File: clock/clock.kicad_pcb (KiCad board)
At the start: 2 copper layers, 100 x 50 mm, 81 parts, among them J1 FTDI, J2 USB, J3 TP, SW1 SW_SPST, SW2 SW_SPST, SW3 SW_SPST, SW4 SW_SPST, SW5 SW_SPST, U1 iv12, U10 PCA9685PW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

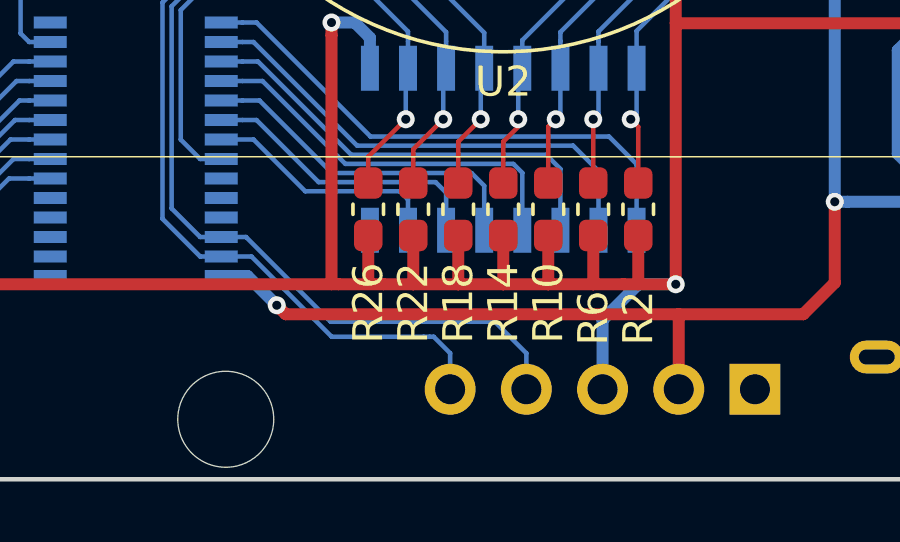
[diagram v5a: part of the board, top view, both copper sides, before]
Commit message: Moved 24v test point
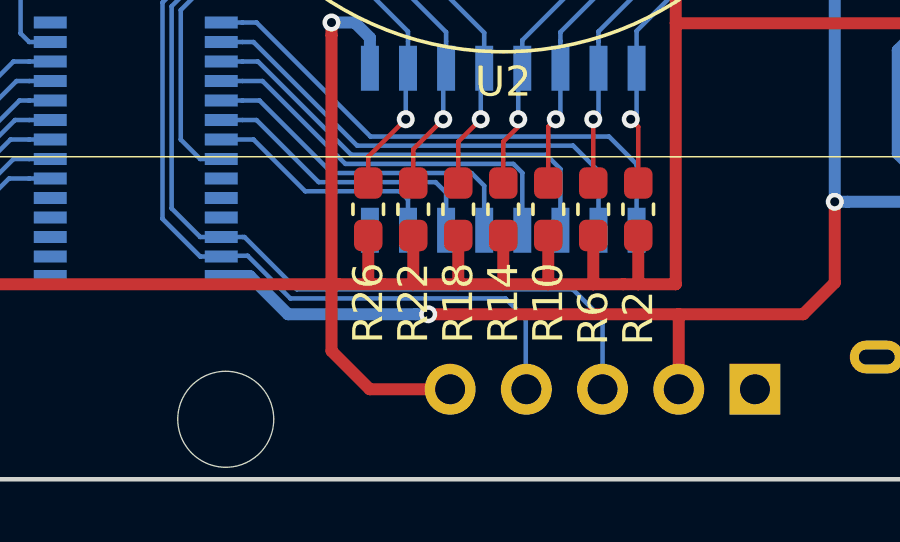
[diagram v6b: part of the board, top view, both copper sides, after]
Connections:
- J3 pad 3: +24V -> SCL
- J3 pad 4: SCL -> SDA
- J3 pad 5: SDA -> +24V
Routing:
- net SDA: track 122.3 -> 125.6 mm
- net SCL: track 126.7 -> 129.9 mm
- net +24V: track 262.7 -> 264.2 mm, vias 7 -> 6
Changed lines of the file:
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@@
     (tags "resistor handsolder")
     (attr smd)
-    (fp_text reference R39 (at 3 0.05) (layer B.SilkS)
+    (fp_text reference R39 (at -3.025 0) (layer B.SilkS)
       (effects (font (size 1 1) (thickness 0.15)) (justify mirror))
     )
@@
     (tags "resistor handsolder")
     (attr smd)
-    (fp_text reference R40 (at -3 0.1 180) (layer B.SilkS)
+    (fp_text reference R40 (at 3.025 0 180) (layer B.SilkS)
       (effects (font (size 1 1) (thickness 0.15)) (justify mirror))
     )
@@
       (net 31 +5V))
     (pad 3 thru_hole oval (at 0 -5.08 90) (size 1.7 1.7) (drill 1) (layers *.Cu *.Mask)
+      (net 73 SCL))
+    (pad 4 thru_hole oval (at 0 -7.62 90) (size 1.7 1.7) (drill 1) (layers *.Cu *.Mask)
+      (net 72 SDA))
+    (pad 5 thru_hole oval (at 0 -10.16 90) (size 1.7 1.7) (drill 1) (layers *.Cu *.Mask)
       (net 2 +24V))
-    (pad 4 thru_hole oval (at 0 -7.62 90) (size 1.7 1.7) (drill 1) (layers *.Cu *.Mask)
-      (net 73 SCL))
-    (pad 5 thru_hole oval (at 0 -10.16 90) (size 1.7 1.7) (drill 1) (layers *.Cu *.Mask)
-      (net 72 SDA))
     (model ${KISYS3DMOD}/Connector_PinHeader_2.54mm.3dshapes/PinHeader_1x05_P2.54mm_Vertical.wrl
       (at (xyz 0 0 0))
@@
   (segment (start 82.75 145.5) (end 82 145.5) (width 0.4) (layer F.Cu) (net 2))
   (segment (start 82 145.5) (end 81.500034 145.000034) (width 0.4) (layer F.Cu) (net 2))
-  (via (at 117.5 145.5) (size 0.6) (drill 0.3) (layers F.Cu B.Cu) (net 2))
   (segment (start 117.5 136.8) (end 117.5 145.5) (width 0.4) (layer F.Cu) (net 2))
   (segment (start 116.25 145.5) (end 117.5 145.5) (width 0.4) (layer F.Cu) (net 2))
-  (segment (start 116.25 145.5) (end 117.5 145.5) (width 0.4) (layer B.Cu) (net 2))
-  (segment (start 115.06 149) (end 115.06 146.69) (width 0.4) (layer B.Cu) (net 2))
-  (segment (start 115.06 146.69) (end 116.25 145.5) (width 0.4) (layer B.Cu) (net 2))
+  (segment (start 106.025 145.5) (end 106.025 147.725) (width 0.4) (layer F.Cu) (net 2))
+  (segment (start 107.3 149) (end 109.98 149) (width 0.4) (layer F.Cu) (net 2))
+  (segment (start 106.025 147.725) (end 107.3 149) (width 0.4) (layer F.Cu) (net 2))
   (via (at 91.49999 140) (size 0.6) (drill 0.3) (layers F.Cu B.Cu) (net 3))
   (segment (start 91.75 142.125) (end 91.75 140.25001) (width 0.152) (layer F.Cu) (net 3) (status 10))
@@
   (segment (start 127 144.15) (end 127 142.75) (width 0.4) (layer B.Cu) (net 31) (status 10))
   (segment (start 128 142.75) (end 127 142.75) (width 0.4) (layer B.Cu) (net 31))
-  (via (at 104.2 146.2) (size 0.6) (drill 0.3) (layers F.Cu B.Cu) (net 31))
-  (segment (start 103.225 145.225) (end 102.35 145.225) (width 0.4) (layer B.Cu) (net 31) (status 20))
-  (segment (start 104.2 146.2) (end 103.225 145.225) (width 0.4) (layer B.Cu) (net 31))
   (via (at 149.4 146.2) (size 0.6) (drill 0.3) (layers F.Cu B.Cu) (net 31))
   (segment (start 150.375 145.225) (end 151.65 145.225) (width 0.4) (layer B.Cu) (net 31) (status 20))
@@
   (segment (start 119.2 119.6) (end 119.2 122.6) (width 0.4) (layer B.Cu) (net 31))
   (segment (start 119.2 122.6) (end 120.25 123.65) (width 0.4) (layer B.Cu) (net 31))
-  (segment (start 104.2 146.2) (end 104.499999 146.499999) (width 0.4) (layer F.Cu) (net 31))
   (segment (start 117.6 149) (end 117.6 146.499999) (width 0.4) (layer F.Cu) (net 31))
-  (segment (start 104.499999 146.499999) (end 117.6 146.499999) (width 0.4) (layer F.Cu) (net 31))
   (segment (start 122.8 145.45) (end 122.8 142.749984) (width 0.4) (layer F.Cu) (net 31))
   (segment (start 117.6 146.499999) (end 121.750001 146.499999) (width 0.4) (layer F.Cu) (net 31))
@@
   (segment (start 126.574999 105.6) (end 121.45 105.6) (width 0.4) (layer B.Cu) (net 31))
   (segment (start 121.45 105.6) (end 119.25 107.8) (width 0.4) (layer B.Cu) (net 31))
+  (segment (start 108.825736 146.499999) (end 109.25 146.499999) (width 0.4) (layer B.Cu) (net 31))
+  (segment (start 103.3 145.225) (end 104.574999 146.499999) (width 0.4) (layer B.Cu) (net 31))
+  (segment (start 117.6 146.499999) (end 109.25 146.499999) (width 0.4) (layer F.Cu) (net 31))
+  (segment (start 102.35 145.225) (end 103.3 145.225) (width 0.4) (layer B.Cu) (net 31))
+  (segment (start 104.574999 146.499999) (end 108.825736 146.499999) (width 0.4) (layer B.Cu) (net 31))
+  (via (at 109.25 146.499999) (size 0.6) (drill 0.3) (layers F.Cu B.Cu) (net 31))
   (segment (start 143.125 132.776301) (end 143.0861 132.815201) (width 0.152) (layer B.Cu) (net 32) (status 30))
   (segment (start 143.125 128.5) (end 143.125 132.776301) (width 0.152) (layer B.Cu) (net 32) (status 30))
@@
   (segment (start 103.3 123.59013) (end 103.3 133.2) (width 0.152) (layer B.Cu) (net 72))
   (segment (start 100.39198 143.31898) (end 101.648 144.575) (width 0.152) (layer B.Cu) (net 72))
-  (segment (start 102.35 144.575) (end 103.356442 144.575) (width 0.152) (layer B.Cu) (net 72))
-  (segment (start 103.356442 144.575) (end 106.031442 147.25) (width 0.152) (layer B.Cu) (net 72))
-  (segment (start 106.031442 147.25) (end 109.1 147.25) (width 0.152) (layer B.Cu) (net 72))
-  (segment (start 109.432081 147.25) (end 109.3 147.25) (width 0.152) (layer B.Cu) (net 72))
-  (segment (start 109.98 147.797919) (end 109.432081 147.25) (width 0.152) (layer B.Cu) (net 72))
-  (segment (start 109.98 149) (end 109.98 147.797919) (width 0.152) (layer B.Cu) (net 72))
-  (segment (start 109.1 147.25) (end 109.3 147.25) (width 0.152) (layer B.Cu) (net 72))
   (segment (start 124.7 113.2) (end 122.75 113.2) (width 0.152) (layer B.Cu) (net 72))
   (via (at 124.7 113.2) (size 0.6) (drill 0.3) (layers F.Cu B.Cu) (net 72))
@@
   (segment (start 116.45 115.175) (end 118.075 115.175) (width 0.152) (layer B.Cu) (net 72))
   (segment (start 118.075 115.175) (end 120.05 113.2) (width 0.152) (layer B.Cu) (net 72))
+  (segment (start 112.5 148.98) (end 112.52 149) (width 0.152) (layer B.Cu) (net 72))
+  (segment (start 102.375 144.55) (end 103.230296 144.55) (width 0.152) (layer B.Cu) (net 72))
+  (segment (start 103.230296 144.55) (end 104.652294 145.971998) (width 0.152) (layer B.Cu) (net 72))
+  (segment (start 104.652294 145.971998) (end 111.821998 145.971998) (width 0.152) (layer B.Cu) (net 72))
+  (segment (start 111.821998 145.971998) (end 112.5 146.65) (width 0.152) (layer B.Cu) (net 72))
+  (segment (start 102.35 144.575) (end 102.375 144.55) (width 0.152) (layer B.Cu) (net 72))
+  (segment (start 112.5 146.65) (end 112.5 148.98) (width 0.152) (layer B.Cu) (net 72))
   (segment (start 110.875066 116.445) (end 103.604011 123.716055) (width 0.152) (layer B.Cu) (net 73))
   (segment (start 116.45 116.445) (end 110.875066 116.445) (width 0.152) (layer B.Cu) (net 73) (status 10))
@@
   (segment (start 100.695991 142.972991) (end 101.648 143.925) (width 0.152) (layer B.Cu) (net 73))
   (segment (start 103.60401 133.325926) (end 100.695991 136.233945) (width 0.152) (layer B.Cu) (net 73))
-  (segment (start 103.175 143.925) (end 102.35 143.925) (width 0.152) (layer B.Cu) (net 73))
-  (segment (start 106 146.75) (end 103.175 143.925) (width 0.152) (layer B.Cu) (net 73))
-  (segment (start 111.472081 146.75) (end 111 146.75) (width 0.152) (layer B.Cu) (net 73))
-  (segment (start 112.52 147.797919) (end 111.472081 146.75) (width 0.152) (layer B.Cu) (net 73))
-  (segment (start 112.52 149) (end 112.52 147.797919) (width 0.152) (layer B.Cu) (net 73))
-  (segment (start 111 146.75) (end 106 146.75) (width 0.152) (layer B.Cu) (net 73))
   (via (at 124.7 112.4) (size 0.6) (drill 0.3) (layers F.Cu B.Cu) (net 73))
   (segment (start 124.7 112.4) (end 122.75 112.4) (width 0.152) (layer B.Cu) (net 73))
@@
   (segment (start 156.648 143.925) (end 153.404011 140.681011) (width 0.152) (layer B.Cu) (net 73))
   (segment (start 141 112.4) (end 141.05 112.45) (width 0.152) (layer F.Cu) (net 73))
+  (segment (start 103.052 143.925) (end 102.35 143.925) (width 0.152) (layer B.Cu) (net 73))
+  (segment (start 103.125 143.925) (end 103.052 143.925) (width 0.152) (layer B.Cu) (net 73))
+  (segment (start 104.867987 145.667987) (end 103.125 143.925) (width 0.152) (layer B.Cu) (net 73))
+  (segment (start 114.067987 145.667987) (end 104.867987 145.667987) (width 0.152) (layer B.Cu) (net 73))
+  (segment (start 115.06 149) (end 115.06 146.66) (width 0.152) (layer B.Cu) (net 73))
+  (segment (start 115.06 146.66) (end 114.067987 145.667987) (width 0.152) (layer B.Cu) (net 73))
   (segment (start 131.15 126.8) (end 131.75 126.2) (width 0.4) (layer B.Cu) (net 81) (status 30))
   (segment (start 131.15 133.4) (end 131.15 126.8) (width 0.4) (layer B.Cu) (net 81) (status 30))

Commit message: Added diode polarity marks
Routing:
- net SDA: track 125.6 -> 126.4 mm
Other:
- board text added: "+"
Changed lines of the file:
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@@
   (general
     (thickness 1.6)
-    (drawings 11)
-    (tracks 902)
+    (drawings 16)
+    (tracks 903)
     (zones 0)
     (modules 81)
@@
     )
   )
+  (gr_text + (at 133.5 124.2) (layer F.SilkS)
+    (effects (font (size 1 1) (thickness 0.15)))
+  )
+  (gr_text + (at 168.8 125.8) (layer F.SilkS)
+    (effects (font (size 1 1) (thickness 0.15)))
+  )
+  (gr_text + (at 144.3 125.8) (layer F.SilkS)
+    (effects (font (size 1 1) (thickness 0.15)))
+  )
+  (gr_text + (at 113.8 125.8) (layer F.SilkS)
+    (effects (font (size 1 1) (thickness 0.15)))
+  )
+  (gr_text + (at 88.8 125.8) (layer F.SilkS)
+    (effects (font (size 1 1) (thickness 0.15)))
+  )
   (gr_text "24v\n" (at 115.1 146.2 270) (layer B.SilkS)
     (effects (font (size 1 1) (thickness 0.15)) (justify mirror))
@@
   (segment (start 124.7 113.2) (end 141 113.2) (width 0.152) (layer F.Cu) (net 72))
   (segment (start 124.7 113.2) (end 121.2 113.2) (width 0.152) (layer F.Cu) (net 72))
-  (segment (start 121.2 113.624264) (end 121.2 113.2) (width 0.152) (layer B.Cu) (net 72))
-  (segment (start 121.2 116.55) (end 121.2 113.624264) (width 0.152) (layer B.Cu) (net 72))
-  (segment (start 123.25 118.6) (end 121.2 116.55) (width 0.152) (layer B.Cu) (net 72))
   (via (at 121.2 113.2) (size 0.6) (drill 0.3) (layers F.Cu B.Cu) (net 72))
   (segment (start 120.05 113.2) (end 121.2 113.2) (width 0.152) (layer B.Cu) (net 72))
@@
   (segment (start 102.35 144.575) (end 102.375 144.55) (width 0.152) (layer B.Cu) (net 72))
   (segment (start 112.5 146.65) (end 112.5 148.98) (width 0.152) (layer B.Cu) (net 72))
+  (segment (start 121.2 113.624264) (end 121.2 113.2) (width 0.152) (layer B.Cu) (net 72))
+  (segment (start 121.2 118) (end 121.2 113.624264) (width 0.152) (layer B.Cu) (net 72))
+  (segment (start 123.25 118.6) (end 121.8 118.6) (width 0.152) (layer B.Cu) (net 72))
+  (segment (start 121.8 118.6) (end 121.2 118) (width 0.152) (layer B.Cu) (net 72))
   (segment (start 110.875066 116.445) (end 103.604011 123.716055) (width 0.152) (layer B.Cu) (net 73))
   (segment (start 116.45 116.445) (end 110.875066 116.445) (width 0.152) (layer B.Cu) (net 73) (status 10))
